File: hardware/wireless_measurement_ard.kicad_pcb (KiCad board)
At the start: 2 copper layers, 50 x 21 mm, 25 parts, among them J1 Conn_01x08, J2 Tag-Connect, SW1 SW_SPDT, U1 EFM8LB1, U2 JDY-08, U3 MCP16415, U4 MAX9938, U5 MAX9938

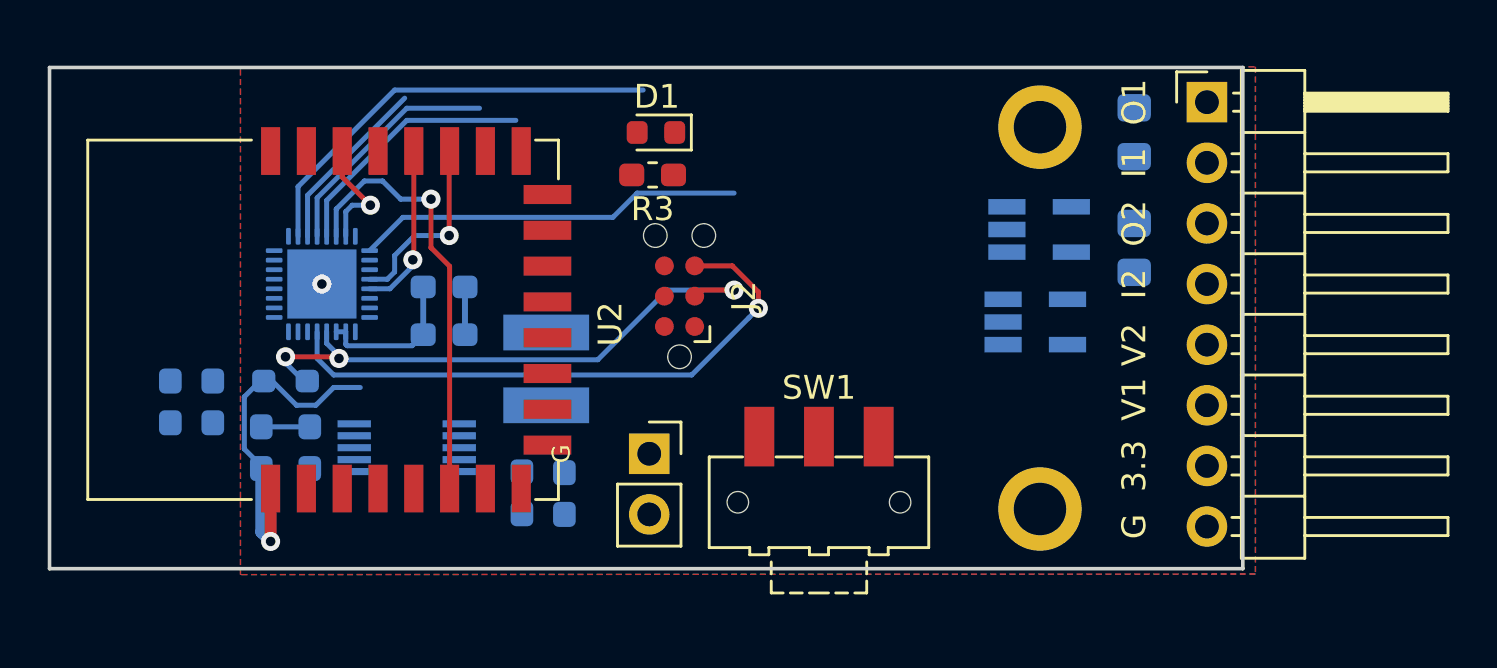
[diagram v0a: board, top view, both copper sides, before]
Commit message: reorg folder and added readme for mini
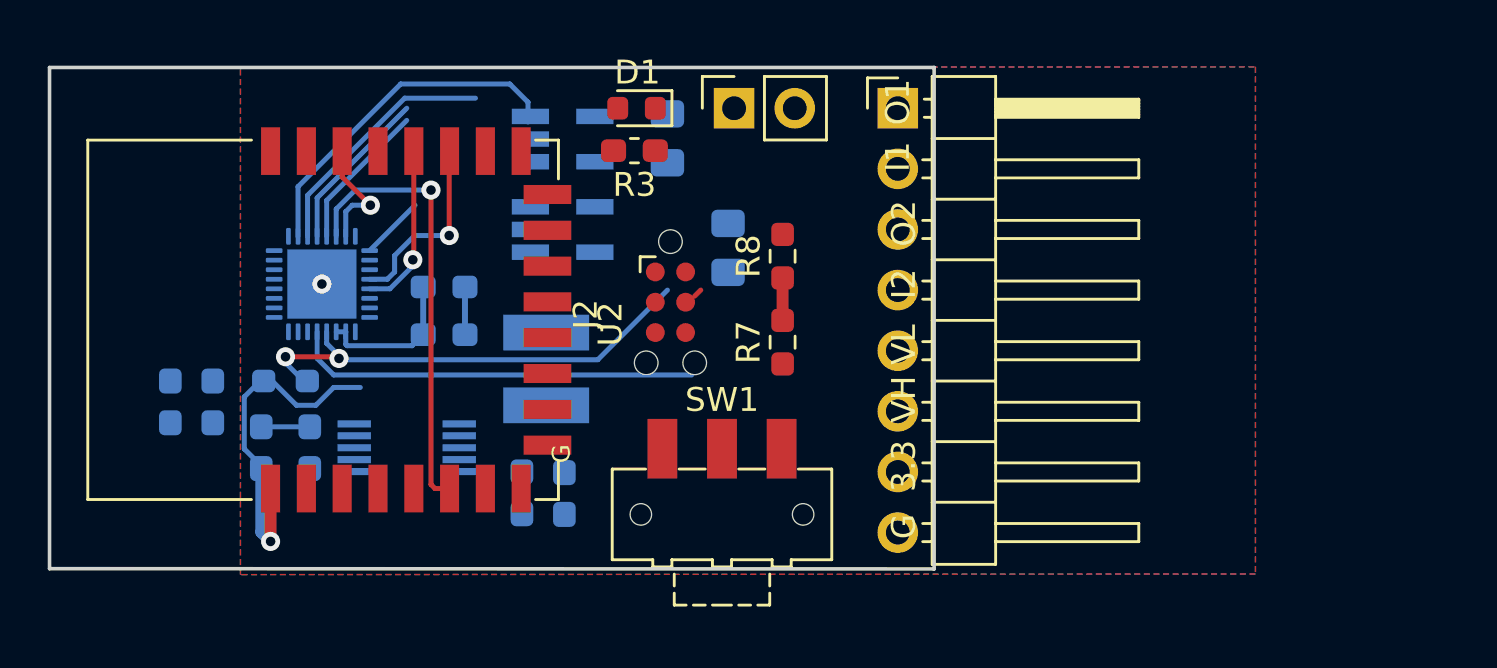
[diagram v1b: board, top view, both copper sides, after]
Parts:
- removed H1, H2: MountingHole_Pad, MountingHole:MountingHole_2.2mm_M2_ISO7380_Pad
- added R7: 110k, Resistor_SMD:R_0603_1608Metric_Pad0.98x0.95mm_HandSolder, F.Cu at (140.7, 86.5)
- added R8: 10k, Resistor_SMD:R_0603_1608Metric_Pad0.98x0.95mm_HandSolder, F.Cu at (140.7, 82.9)
- moved U4 20.3 mm to (131.5, 78.0)
- moved U5 20.2 mm to (131.5, 81.8)
- moved R1 19.6 mm to (135.9, 78.0)
- moved R2 17.0 mm to (138.4, 82.6)
- moved Battery1 14.9 mm to (138.7, 76.7), turned to 90 degrees
- moved J1 13.0 mm to (145.5, 76.7)
- moved SW1 4.10 mm to (138.2, 93.7)
- moved D1 1.30 mm to (134.6, 76.7)
- moved R3 1.27 mm to (134.5, 78.5)
- moved J2 0.46 mm to (136.0, 84.8), turned to 270 degrees
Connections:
- J1 pad 6: A3 -> VHIGH
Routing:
- net LED: track 16.3 -> 2.69 mm
- net C2D: track 24.9 -> 17.1 mm, vias 1 -> 0
- net C2CK: track 24.6 -> 20.5 mm, vias 3 -> 2
- net A0: track 18.2 -> 14.6 mm
- net A2: track 9.97 -> 6.92 mm
- net A1: track 7.47 -> 10.4 mm
- net A3: track 10.8 -> 8.03 mm
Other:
- board size 50 x 21 mm -> 37.1 x 21 mm
- board text added: "VH"
- board text added: "VL"
- board text removed: "V1"
- board text removed: "V2"

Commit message: completed v1
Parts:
- removed R2: 5R3, Resistor_SMD:R_0805_2012Metric_Pad1.15x1.40mm_HandSolder
- removed U5: MAX9938, Package_TO_SOT_SMD:SOT-23-5_HandSoldering
- R1: value 5R3 -> 1R
- SW1: moved to B.Cu
- U4: value MAX9938 -> MAX44284; footprint Package_TO_SOT_SMD:SOT-23-5_HandSoldering -> Package_TO_SOT_SMD:SOT-23-6_Handsoldering
- moved Battery1 25.0 mm to (122.4, 95.8)
- moved SW1 23.2 mm to (115.1, 95.8), turned to 180 degrees
- moved J2 11.8 mm to (131.1, 95.5), turned to 0 degrees
- moved J1 8.64 mm to (137.0, 77.7)
- moved R6 7.92 mm to (125.5, 93.7)
- moved R7 7.25 mm to (133.9, 88.8)
- moved R8 7.24 mm to (133.8, 85.1)
- moved U2 2.05 mm to (120.4, 83.8)
- moved C5 1.79 mm to (126.4, 86.0)
- moved C6 1.57 mm to (126.4, 87.8)
- moved R3 1.53 mm to (133.5, 79.6), turned to 270 degrees
- moved R1 1.48 mm to (134.6, 78.7)
- moved D1 1.27 mm to (133.3, 77.0)
- moved U4 1.22 mm to (130.5, 78.7), turned to 180 degrees
- moved C1 0.89 mm to (116.0, 89.0)
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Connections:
- J1 pad 1: C1_OUT -> C1_IN
- J1 pad 2: C1_IN -> C1_OUT
- J1 pad 3: C2_OUT -> A1
- J1 pad 4: C2_IN -> A2
- J1 pad 5: A2 -> VHIGH
- J1 pad 6: VHIGH -> A4
- R1 pad 1: C1_IN -> C1_OUT
- R1 pad 2: C1_OUT -> C1_IN
- U1 pad 26: Net-(U1-Pad26) -> A4
- U4 pad 1: GND -> +3V3
- U4 pad 3: A0 -> C1_IN
- U4 pad 5: C1_IN -> A0
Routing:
- net GND: track 2.00 -> 59.3 mm, vias 1 -> 4
- net +3V3: track 21.2 -> 77.0 mm, vias 1 -> 4
- net VIN: track 0.00 -> 33.2 mm, vias 0 -> 3
- net A4: track 0.00 -> 18.5 mm
- net A3: track 8.03 -> 25.7 mm, vias 0 -> 1
- net A2: track 6.92 -> 23.3 mm
- net BATT: track 0.00 -> 15.2 mm
- net LED: track 2.69 -> 17.7 mm, vias 0 -> 1
- net A1: track 10.4 -> 21.7 mm
- net C1_OUT: track 0.00 -> 7.89 mm
- net C1_IN: track 0.00 -> 6.34 mm
- net VHIGH: track 0.00 -> 3.96 mm
- net Net-(L1-Pad2): track 0.00 -> 3.71 mm
- net ARD_TX: track 7.03 -> 10.7 mm
- net C2D: track 17.1 -> 20.8 mm, vias 0 -> 1
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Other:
- board size 37.1 x 21 mm -> 30 x 23 mm
- board text added: "+"
- board text added: "-"
- board text added: "A1"
- board text added: "A2"
- board text added: "A4"
- board text added: "SWM-mini Sep 21"
- board text removed: "I2"
- board text removed: "O2"
- board text removed: "SWM-mini Aug 21"
- board text removed: "VL"

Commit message: mini version
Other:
- rule pad_to_mask_clearance: 0.05 -> 0

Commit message: fixed powersupply
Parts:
- added C : 4.7uF, Capacitor_SMD:C_0603_1608Metric_Pad1.08x0.95mm_HandSolder, B.Cu at (126.3, 84.3)
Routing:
- net GND: track 59.3 -> 73.2 mm
- net Net-(C7-Pad2): track 0.00 -> 3.55 mm
- net +3V3: track 77.0 -> 78.7 mm
- net ARD_TX: track 10.7 -> 9.26 mm
- net ARD_RX: track 11.7 -> 12.7 mm
- net A4: track 18.5 -> 19.1 mm
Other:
- board text added: "OFF"
- board text added: "ON"

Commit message: fix added changes to pcb
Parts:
- C7: renamed from C 
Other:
- board text added: "SWM-mini-2 Sep 21"
- board text removed: "SWM-mini Sep 21"
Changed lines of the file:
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@@
   (general
     (thickness 1.6)
-    (drawings 18)
+    (drawings 17)
     (tracks 297)
     (zones 0)
@@
     (35 F.Paste user)
     (36 B.SilkS user)
-    (37 F.SilkS user)
+    (37 F.SilkS user hide)
     (38 B.Mask user)
     (39 F.Mask user)
@@
     (tags "capacitor handsolder")
     (attr smd)
-    (fp_text reference "C " (at 0 1.43) (layer B.SilkS)
+    (fp_text reference C7 (at 0 1.43) (layer B.SilkS)
       (effects (font (size 1 1) (thickness 0.15)) (justify mirror))
     )
@@
     (tags "capacitor handsolder")
     (attr smd)
-    (fp_text reference C5 (at 0.141 -1.524) (layer B.SilkS)
-      (effects (font (size 1 1) (thickness 0.15)) (justify mirror))
+    (fp_text reference C5 (at -1.891 0.127 90) (layer B.SilkS)
+      (effects (font (size 0.5 0.5) (thickness 0.1)) (justify mirror))
     )
     (fp_text value 4.7uF (at 0 -1.43 180) (layer B.Fab)
@@
     (effects (font (size 1 1) (thickness 0.15)) (justify mirror))
   )
-  (gr_text G (at 131.445 91.186 90) (layer F.SilkS)
-    (effects (font (size 0.75 0.75) (thickness 0.15)))
-  )
-  (gr_text "SWM-mini\nSep 21\n" (at 113.792 81.915 90) (layer B.SilkS)
-    (effects (font (size 1.5 1.5) (thickness 0.3)) (justify mirror))
+  (gr_text "SWM-mini-2\nSep 21\n" (at 112.776 75.184 90) (layer B.SilkS)
+    (effects (font (size 1.5 1.5) (thickness 0.3)) (justify left mirror))
   )
   (gr_line (start 110 98) (end 110 75) (layer Edge.Cuts) (width 0.15))

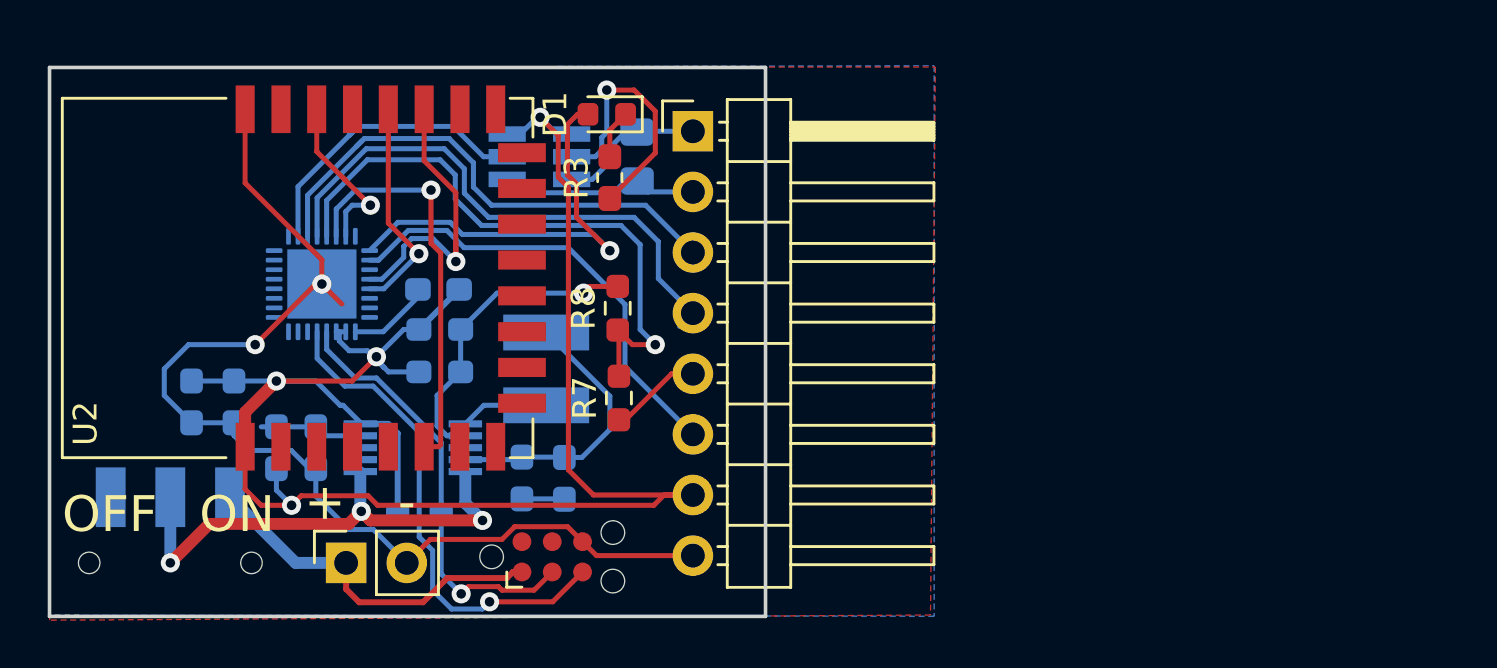
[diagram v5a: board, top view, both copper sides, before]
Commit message: added bidrectional current flow
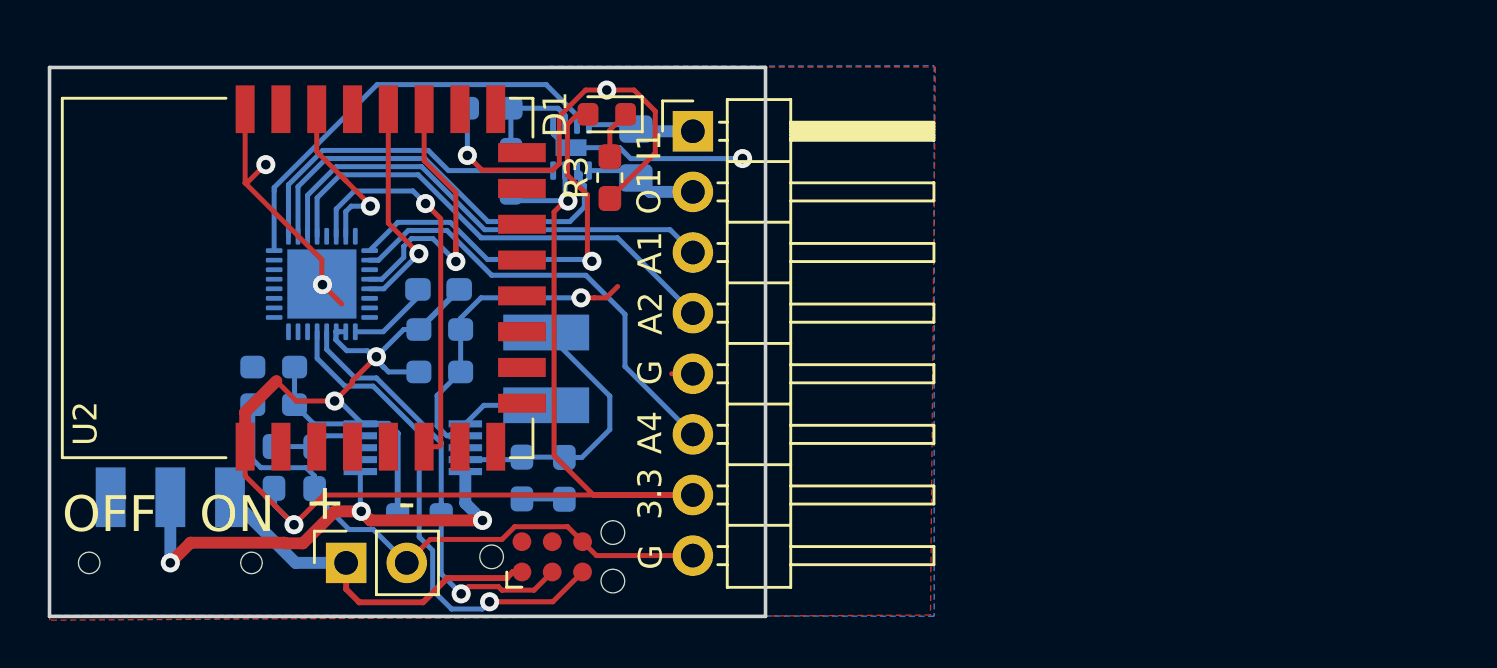
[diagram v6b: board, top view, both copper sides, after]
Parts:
- R7: moved to B.Cu
- R8: value 10k -> 110k; moved to B.Cu
- U4: value MAX44284 -> MAX40204_TFN; footprint Package_TO_SOT_SMD:SOT-23-6_Handsoldering -> Package_DFN_QFN:DFN-8-1EP_2x2mm_P0.5mm_EP0.7x1.3mm
- moved R7 10.5 mm to (129.3, 79.4)
- moved R8 9.96 mm to (128.4, 76.7), turned to 180 degrees
- moved C1 3.74 mm to (119.4, 87.6), turned to 180 degrees
- moved C2 1.67 mm to (119.4, 89.1), turned to 180 degrees
- moved U4 1.38 mm to (131.9, 78.4), turned to 270 degrees
- moved R5 0.84 mm to (121.1, 91.8)
- moved R4 0.83 mm to (119.4, 91.8)
- moved R1 0.14 mm to (134.6, 78.6), turned to 270 degrees
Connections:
- J1 pad 1: C1_IN -> C1_OUT
- J1 pad 2: C1_OUT -> C1_IN
- R7 pad 1: VHIGH -> +3V3
- R7 pad 2: A3 -> Net-(R7-Pad2)
- R8 pad 1: A3 -> Net-(R7-Pad2)
- U1 pad 16: Net-(U1-Pad16) -> GAIN
- U1 pad 17: Net-(U1-Pad17) -> MAX_SHDN
- U1 pad 21: A3 -> Net-(U1-Pad21)
- U4 pad 1: +3V3 -> GND
- U4 pad 2: GND -> Net-(R7-Pad2)
- U4 pad 3: C1_IN -> GAIN
- U4 pad 5: A0 -> C1_IN
- U4 pad 6: +3V3 -> A0
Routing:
- net A3: track 25.7 -> 0.00 mm, vias 1 -> 0
- net GAIN: track 0.00 -> 18.0 mm
- net MAX_SHDN: track 0.00 -> 14.2 mm
- net A0: track 12.6 -> 17.6 mm
- net Net-(R7-Pad2): track 0.00 -> 4.51 mm
- net +3V3: track 78.7 -> 74.8 mm
- net GND: track 73.2 -> 76.9 mm, vias 4 -> 6
- net C1_OUT: track 7.89 -> 4.47 mm
- net VHIGH: track 3.96 -> 0.96 mm
- net A2: track 23.3 -> 20.9 mm
- net A1: track 21.7 -> 19.8 mm
- net C1_IN: track 6.34 -> 4.72 mm
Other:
- board text added: "SWM-mini-3 Oct 21"
- board text removed: "SWM-mini-2 Sep 21"
- board text removed: "VH"

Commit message: Added WSL footprint
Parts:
- U4: value MAX40204_TFN -> MAX40204; footprint Package_DFN_QFN:DFN-8-1EP_2x2mm_P0.5mm_EP0.7x1.3mm -> ben_common:BGA-8_4x2_1.468x0.848mm
- moved R8 4.92 mm to (131.8, 80.3)
- moved U4 0.39 mm to (131.8, 78.0), turned to 180 degrees
- moved R7 0.24 mm to (129.1, 79.4), turned to 270 degrees
- turned R1 to 90 degrees
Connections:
- J1 pad 1: C1_OUT -> C1_IN
- J1 pad 2: C1_IN -> C1_OUT
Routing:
- net GND: track 76.9 -> 71.2 mm, vias 6 -> 7
- net +3V3: track 74.8 -> 79.3 mm
- net Net-(R7-Pad2): track 4.51 -> 8.17 mm
- net A0: track 17.6 -> 15.3 mm, vias 0 -> 2
- net LED: track 17.7 -> 18.8 mm
- net C1_OUT: track 4.47 -> 5.48 mm
- net STATUS: track 16.5 -> 15.5 mm
- net PWRC: track 7.39 -> 8.09 mm
- net MAX_SHDN: track 14.2 -> 14.8 mm
